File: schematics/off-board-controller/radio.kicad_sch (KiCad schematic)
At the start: 2 parts, among them J2 5-1814832-1, U5 RFM98W-433S2

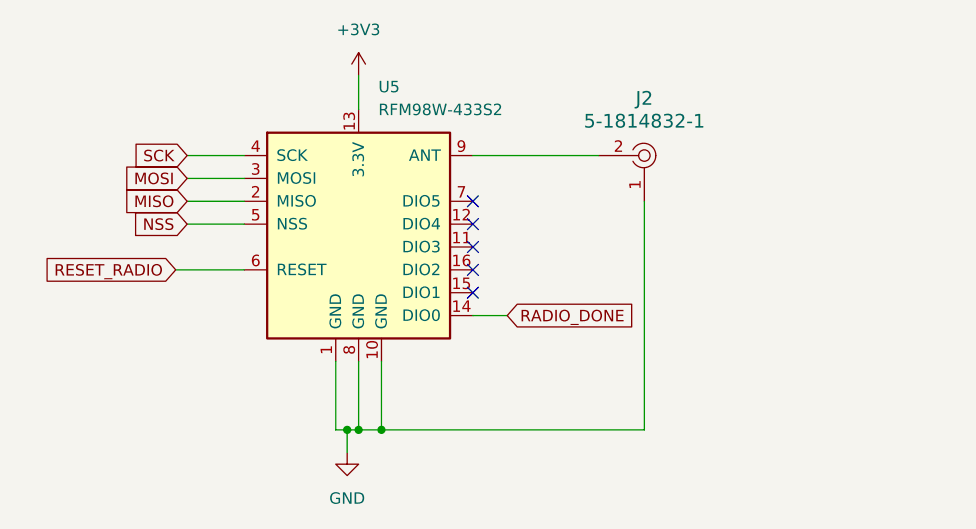
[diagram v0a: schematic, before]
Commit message: off-board: created schematic
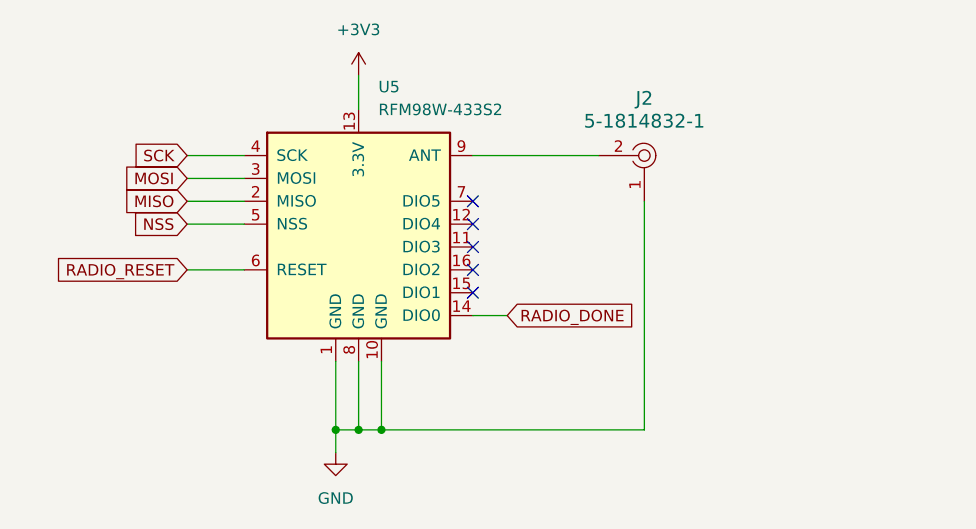
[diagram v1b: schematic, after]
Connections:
- net RESET_RADIO renamed RADIO_RESET
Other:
- title: (none) -> Off-board Controller
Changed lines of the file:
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@@
 	(generator_version "8.0")
 	(paper "A4")
+	(title_block
+		(title "Off-board Controller")
+		(date "2024-07-20")
+	)
 	(junction
-		(at 137.16 107.95)
+		(at 135.89 107.95)
 		(diameter 0)
 		(color 0 0 0 0)
@@
 	(wire
 		(pts
-			(xy 137.16 107.95) (xy 138.43 107.95)
-		)
-		(stroke
-			(width 0)
-			(type default)
-		)
-	)
-	(wire
-		(pts
-			(xy 135.89 107.95) (xy 137.16 107.95)
+			(xy 135.89 107.95) (xy 138.43 107.95)
 		)
 		(stroke
@@
 	(wire
 		(pts
-			(xy 137.16 110.49) (xy 137.16 107.95)
+			(xy 135.89 110.49) (xy 135.89 107.95)
 		)
 		(stroke
@@
 	(wire
 		(pts
-			(xy 118.11 90.17) (xy 125.73 90.17)
+			(xy 119.38 90.17) (xy 125.73 90.17)
 		)
 		(stroke
@@
 		)
 	)
-	(global_label "RESET_RADIO"
+	(global_label "RADIO_RESET"
 		(shape input)
-		(at 118.11 90.17 180)
+		(at 119.38 90.17 180)
 		(fields_autoplaced yes)
 		(effects
@@
 		)
 		(property "Intersheetrefs" "${INTERSHEET_REFS}"
-			(at 102.8482 90.17 0)
+			(at 104.1182 90.17 0)
 			(effects
 				(font
@@
 	(symbol
 		(lib_id "power:GND")
-		(at 137.16 110.49 0)
+		(at 135.89 110.49 0)
 		(unit 1)
 		(exclude_from_sim no)
@@
 		(fields_autoplaced yes)
 		(property "Reference" "#PWR07"
-			(at 137.16 116.84 0)
+			(at 135.89 116.84 0)
 			(effects
 				(font
@@
 		)
 		(property "Value" "GND"
-			(at 137.16 115.57 0)
+			(at 135.89 115.57 0)
 			(effects
 				(font
@@
 		)
 		(property "Footprint" ""
-			(at 137.16 110.49 0)
+			(at 135.89 110.49 0)
 			(effects
 				(font
@@
 		)
 		(property "Datasheet" ""
-			(at 137.16 110.49 0)
+			(at 135.89 110.49 0)
 			(effects
 				(font
@@
 		)
 		(property "Description" "Power symbol creates a global label with name \"GND\" , ground"
-			(at 137.16 110.49 0)
-			(effects
-				(font
+			(at 135.89 110.49 0)
+			(effects
+				(font

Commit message: finished footprints, schematic, and started layout
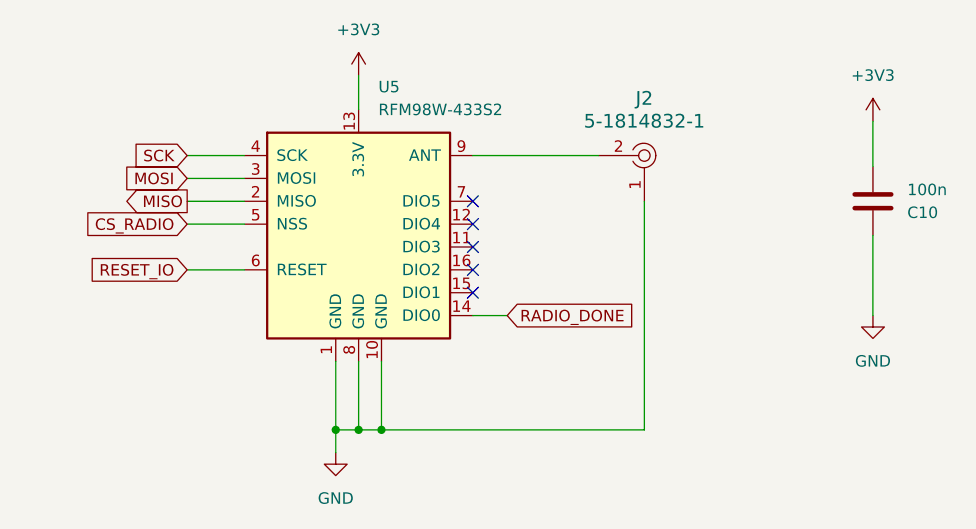
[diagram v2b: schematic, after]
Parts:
- added C10: 100n, Capacitor_SMD:C_0805_2012Metric_Pad1.18x1.45mm_HandSolder, symbol Device:C
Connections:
- net +3V3: now also C10.2
- net GND: now also C10.1
- net NSS renamed CS_RADIO
- net RADIO_RESET renamed RESET_IO
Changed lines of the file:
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@@
+	(wire
+		(pts
+			(xy 195.58 73.66) (xy 195.58 78.74)
+		)
+		(stroke
+			(width 0)
+			(type default)
+		)
+	)
+	(wire
+		(pts
+			(xy 195.58 95.25) (xy 195.58 86.36)
+		)
+		(stroke
+			(width 0)
+			(type default)
+		)
+	)
 	(wire
 		(pts
@@
 		)
 	)
-	(global_label "NSS"
+	(global_label "CS_RADIO"
 		(shape input)
 		(at 119.38 85.09 180)
@@
 		)
 		(property "Intersheetrefs" "${INTERSHEET_REFS}"
-			(at 112.6453 85.09 0)
+			(at 107.3838 85.09 0)
 			(effects
 				(font
@@
 	)
 	(global_label "MISO"
-		(shape input)
+		(shape output)
 		(at 119.38 82.55 180)
 		(fields_autoplaced yes)
@@
 		)
 	)
-	(global_label "RADIO_RESET"
+	(global_label "RESET_IO"
 		(shape input)
 		(at 119.38 90.17 180)
@@
 		)
 		(property "Intersheetrefs" "${INTERSHEET_REFS}"
-			(at 104.1182 90.17 0)
+			(at 107.7468 90.17 0)
 			(effects
 				(font
@@
 				(justify left)
 				(hide yes)
+			)
+		)
+	)
+	(symbol
+		(lib_id "power:GND")
+		(at 195.58 95.25 0)
+		(unit 1)
+		(exclude_from_sim no)
+		(in_bom yes)
+		(on_board yes)
+		(dnp no)
+		(fields_autoplaced yes)
+		(property "Reference" "#PWR022"
+			(at 195.58 101.6 0)
+			(effects
+				(font
+					(size 1.27 1.27)
+				)
+				(hide yes)
+			)
+		)
+		(property "Value" "GND"
+			(at 195.58 100.33 0)
+			(effects
+				(font
+					(size 1.27 1.27)
+				)
+			)
+		)
+		(property "Footprint" ""
+			(at 195.58 95.25 0)
+			(effects
+				(font
+					(size 1.27 1.27)
+				)
+				(hide yes)
+			)
+		)
+		(property "Datasheet" ""
+			(at 195.58 95.25 0)
+			(effects
+				(font
+					(size 1.27 1.27)
+				)
+				(hide yes)
+			)
+		)
+		(property "Description" "Power symbol creates a global label with name \"GND\" , ground"
+			(at 195.58 95.25 0)
+			(effects
+				(font
+					(size 1.27 1.27)
+				)
+				(hide yes)
+			)
+		)
+		(pin "1"
+		)
+		(instances
+			(project "controller"
+				(path "/0775f04a-8a0e-41f5-b442-dacb2efdb863/75911a2a-67a3-4491-aa2f-c0cb98fc09a7"
+					(reference "#PWR022")
+					(unit 1)
+				)
 			)
 		)
@@
 	)
 	(symbol
+		(lib_id "Device:C")
+		(at 195.58 82.55 0)
+		(mirror x)
+		(unit 1)
+		(exclude_from_sim no)
+		(in_bom yes)
+		(on_board yes)
+		(dnp no)
+		(fields_autoplaced yes)
+		(property "Reference" "C10"
+			(at 199.39 83.8201 0)
+			(effects
+				(font
+					(size 1.27 1.27)
+				)
+				(justify left)
+			)
+		)
+		(property "Value" "100n"
+			(at 199.39 81.2801 0)
+			(effects
+				(font
+					(size 1.27 1.27)
+				)
+				(justify left)
+			)
+		)
+		(property "Footprint" "Capacitor_SMD:C_0805_2012Metric_Pad1.18x1.45mm_HandSolder"
+			(at 196.5452 78.74 0)
+			(effects
+				(font
+					(size 1.27 1.27)
+				)
+				(hide yes)
+			)
+		)
+		(property "Datasheet" "~"
+			(at 195.58 82.55 0)
+			(effects
+				(font
+					(size 1.27 1.27)
+				)
+				(hide yes)
+			)
+		)
+		(property "Description" "Unpolarized capacitor"
+			(at 195.58 82.55 0)
+			(effects
+				(font
+					(size 1.27 1.27)
+				)
+				(hide yes)
+			)
+		)
+		(pin "1"
+		)
+		(pin "2"
+		)
+		(instances
+			(project "controller"
+				(path "/0775f04a-8a0e-41f5-b442-dacb2efdb863/75911a2a-67a3-4491-aa2f-c0cb98fc09a7"
+					(reference "C10")
+					(unit 1)
+				)
+			)
+		)
+	)
+	(symbol
 		(lib_id "power:GND")
 		(at 135.89 110.49 0)
@@
 					(unit 1)
 				)
+			)
+		)
+	)
+	(symbol
+		(lib_id "power:+3V3")
+		(at 195.58 73.66 0)
+		(unit 1)
+		(exclude_from_sim no)
+		(in_bom yes)
+		(on_board yes)
+		(dnp no)
+		(fields_autoplaced yes)
+		(property "Reference" "#PWR021"
+			(at 195.58 77.47 0)
+			(effects
+				(font
+					(size 1.27 1.27)
+				)
+				(hide yes)
+			)
+		)
+		(property "Value" "+3V3"
+			(at 195.58 68.58 0)
+			(effects
+				(font
+					(size 1.27 1.27)
+				)
+			)
+		)
+		(property "Footprint" ""
+			(at 195.58 73.66 0)
+			(effects
+				(font
+					(size 1.27 1.27)
+				)
+				(hide yes)
+			)
+		)
+		(property "Datasheet" ""
+			(at 195.58 73.66 0)
+			(effects
+				(font
+					(size 1.27 1.27)
+				)
+				(hide yes)
+			)
+		)
+		(property "Description" "Power symbol creates a global label with name \"+3V3\""
+			(at 195.58 73.66 0)
+			(effects
+				(font
+					(size 1.27 1.27)
+				)
+				(hide yes)
+			)
+		)
+		(pin "1"
+		)
+		(instances
+			(project "controller"
+				(path "/0775f04a-8a0e-41f5-b442-dacb2efdb863/75911a2a-67a3-4491-aa2f-c0cb98fc09a7"
+					(reference "#PWR021")
+					(unit 1)
+				)
